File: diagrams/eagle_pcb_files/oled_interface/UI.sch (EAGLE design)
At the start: 19 parts, among them Q1 BCX59SMD, Q2 BCX59SMD

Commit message: make routing in UI more home-made-possible
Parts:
- R1, R2, R3, R5, R6: value (none) -> 10k
- R4: value (none) -> 10R
- R7: value (none) -> 200R
- renumbered U$1 to OLED
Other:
- note added: "OLED"

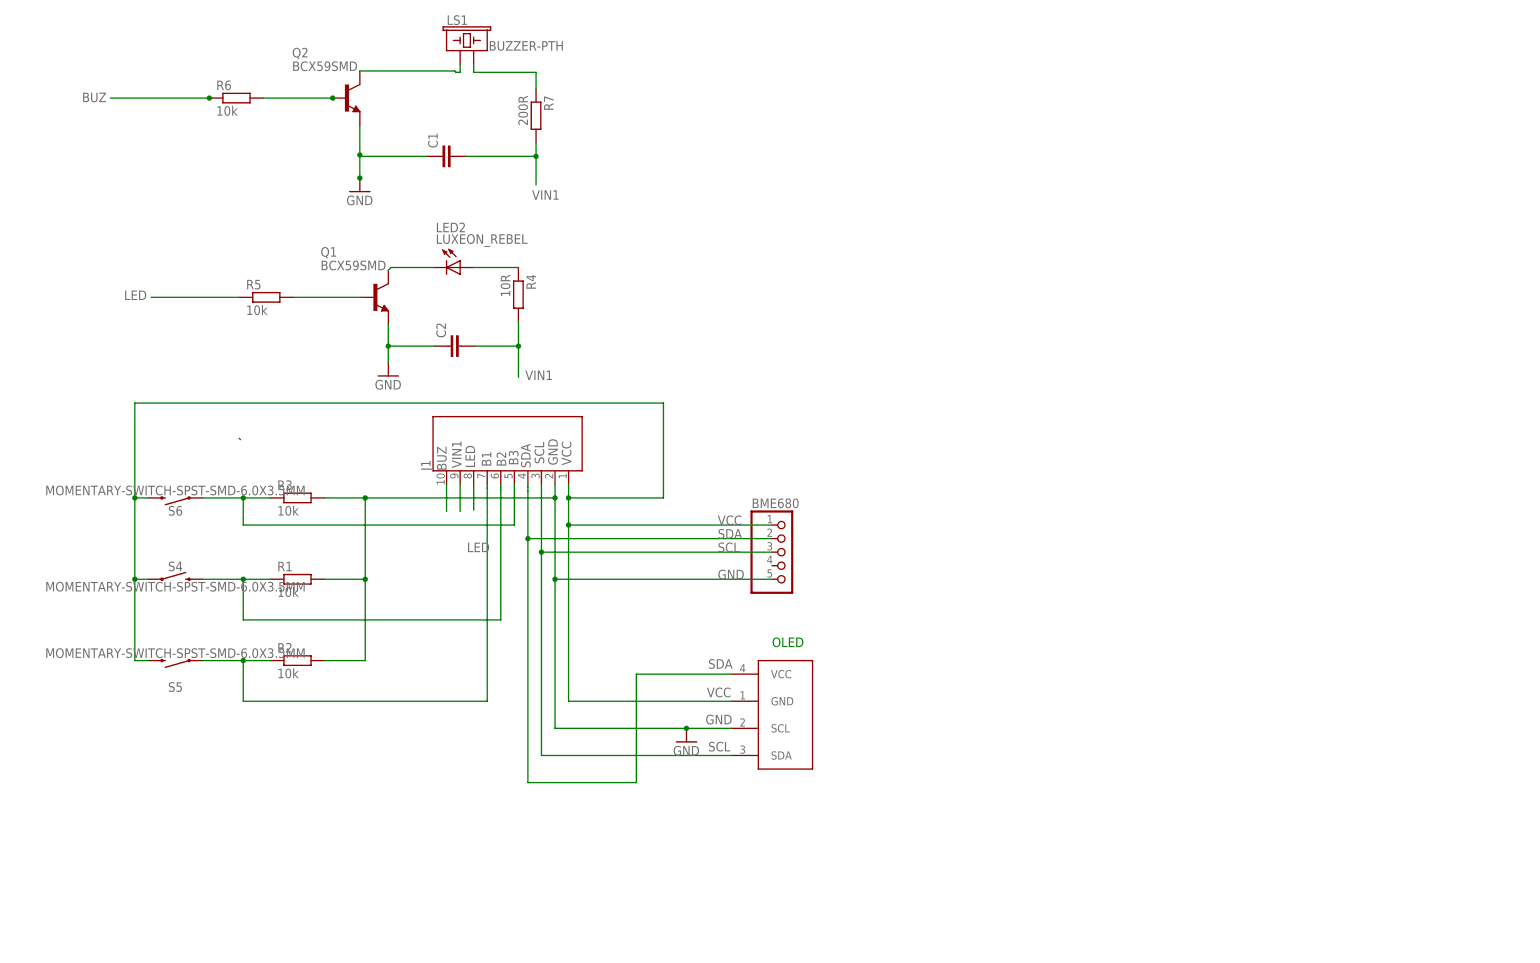
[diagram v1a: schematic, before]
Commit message: oled ready for production
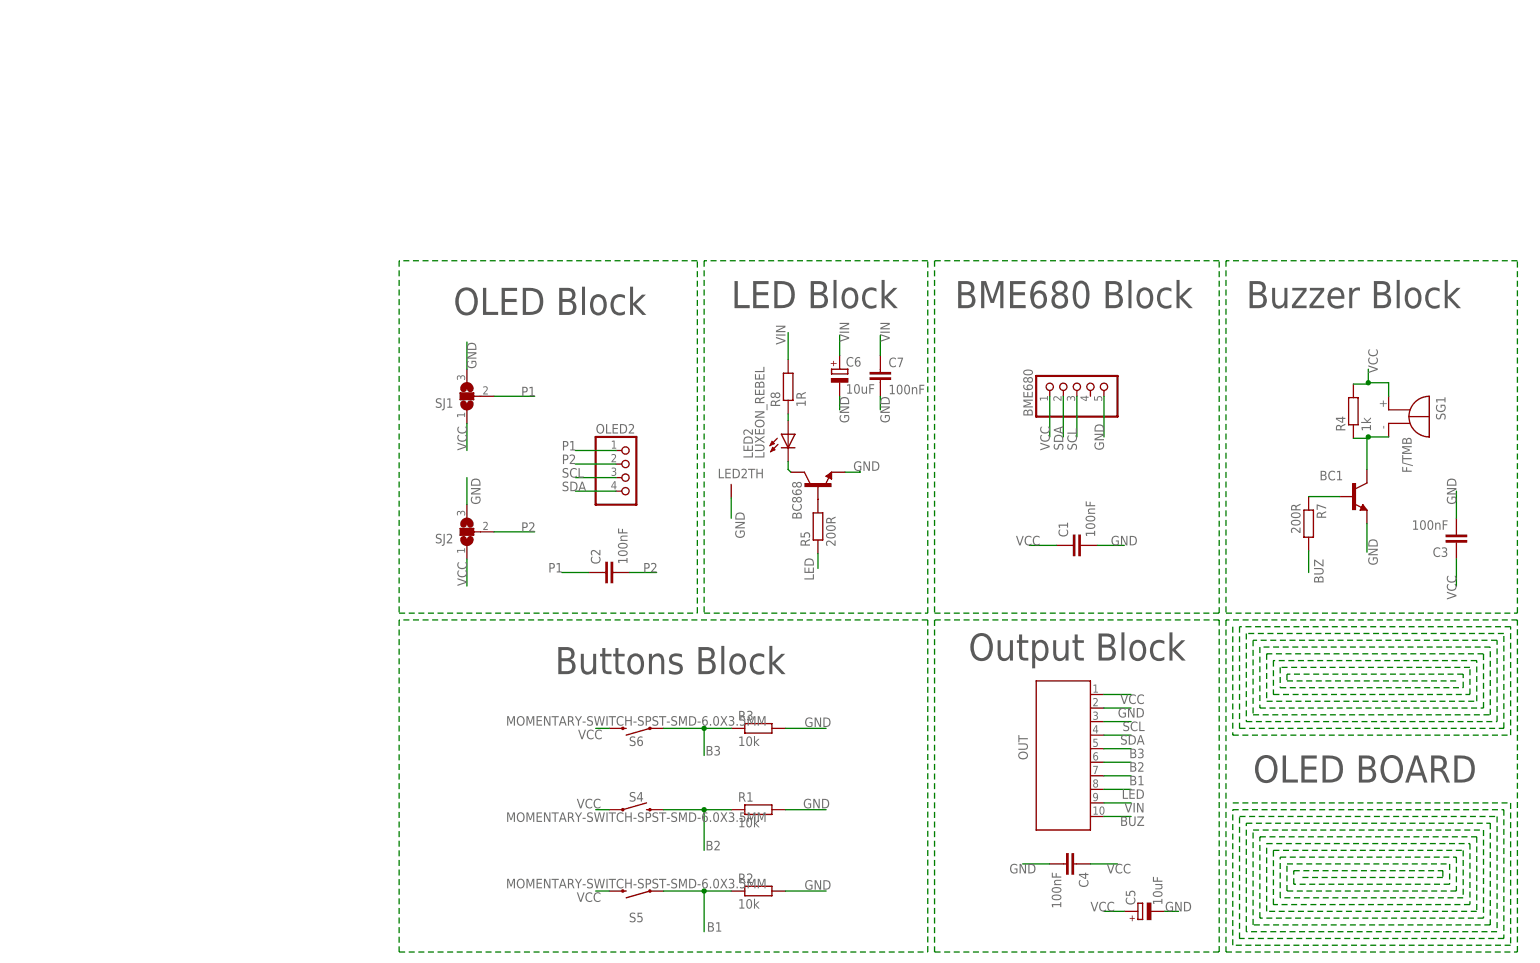
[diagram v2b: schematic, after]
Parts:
- removed J1: (no value), Wurth_Elektronik_Electromechanic_FPC_Connectors_&_Flat_Flexible_Cable_rev18c:686110183422
- removed LS1: BUZZER-PTH, SparkFun-Electromechanical:BUZZER-PTH
- removed OLED: I2C_OLED, DIYMall_OLED:I2C_OLED
- removed Q1, Q2: BCX59SMD, transistor-npn:BCX59SMD
- removed R6: 10k, rcl:R-EU_M1206
- added BC1, BC868: (no value), transistor:BC868-NPN-SOT89-BCE
- added C3, C7: 100nF, rcl:C-EUC0805
- added C4: 100nF, rcl:C-EUC1808
- added C5, C6: 10uF, rcl:CPOL-EUSMCA
- added OLED2: (no value), pinhead:PINHD-1X4
- added OUT: (no value), Wurth_Elektronik_Electromechanic_FPC_Connectors_&_Flat_Flexible_Cable_rev18c:686110183422
- added R8: 1R, eagle-ltspice:RR3216
- added SG1: F/TMB, buzzer:F/TMB
- added SJ1, SJ2: (no value), jumper:SJ2W
- C1, C2: value 0.1UF-0402-16V-10% -> 100nF; device SparkFun-Capacitors:0.1UF-0402-16V-10% -> rcl:C-EUC0805
- R4: value 10R -> 1k; device rcl:R-EU_M1206 -> rcl:R-EU_M0805
- R5: value 10k -> 200R; device rcl:R-EU_M1206 -> rcl:R-EU_M0805
- R7: device rcl:R-EU_M1206 -> rcl:R-EU_M0805
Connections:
- removed net N$9: LS1.1, Q2.C
- removed net VIN1: C1.2, C2.2, J1.2, R4.2, R7.2
- new net P1: C2.1, OLED2.1, SJ1.2
- new net P2: C2.2, OLED2.2, SJ2.2
- new net VIN: C6.+, C7.1, OUT.2, R8.2
- net B1: now also OUT.4; no longer J1.4
- net B2: now also OUT.5; no longer J1.5
- net B3: now also OUT.6; no longer J1.6
- net BUZ: now also OUT.1, R7.2; no longer J1.1, R6.1
- net GND: now also BC1.E, BC868.E, C1.2, C3.2, C4.2, C5.-, C6.-, C7.2, LED2TH.TH, OUT.9, SJ1.3, SJ2.3; no longer C1.1, C2.1, J1.9, OLED.SCL, Q1.E, Q2.E
- net LED: now also OUT.3; no longer J1.3
- net N$1: now also R8.1; no longer R4.1
- net N$2: now also BC868.C; no longer Q1.C
- net N$3: now also BC868.B; no longer Q1.B
- net N$7: now also BC1.B, R7.1; no longer Q2.B, R6.2
- net N$8: now also BC1.C, R4.1, SG1.-; no longer LS1.2, R7.1
- net SCL: now also OLED2.3, OUT.8; no longer J1.8, OLED.SDA
- net SDA: now also OLED2.4, OUT.7; no longer J1.7, OLED.VCC
- net VCC: now also C1.1, C3.1, C4.1, C5.+, OUT.10, R4.2, SG1.+, SJ1.1, SJ2.1; no longer J1.10, OLED.GND
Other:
- note added: "BME680 Block"
- note added: "Buttons Block"
- note added: "Buzzer Block"
- note added: "LED Block"
- note added: "OLED BOARD"
- note added: "OLED Block"
- note added: "Output Block"
- note removed: "GND"
- note removed: "OLED"
- note removed: "SCL"
- note removed: "SDA"
- note removed: "VCC"
- moved on the sheet: BME680, C1, C2, LED2, R1, R2, R3, R4, R5, R7, S4, S5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
